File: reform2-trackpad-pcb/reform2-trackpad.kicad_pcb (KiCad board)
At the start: 2 copper layers, 45 x 21 mm, 26 parts, among them J1 Conn_USB, J2 Conn_01x06_Female, SW6 SW_RST, SW7 SW_HWB, U1 ATmega32U2-AU, U2 TLV75533PDBV, U3 USBLC6-2SC6, Y1 Crystal_GND24

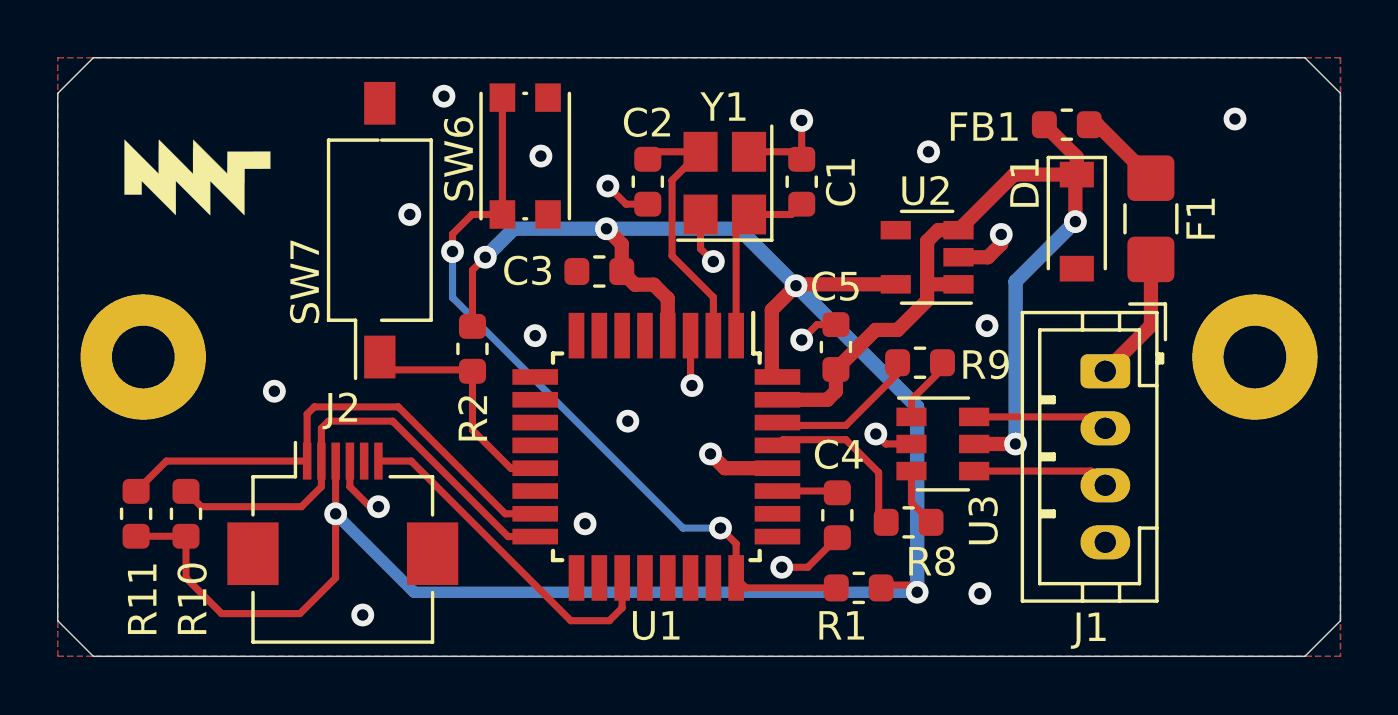
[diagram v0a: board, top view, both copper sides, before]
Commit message: reform2: update PCBs incl. badges to production revs, add keyboard lettering, misc docs
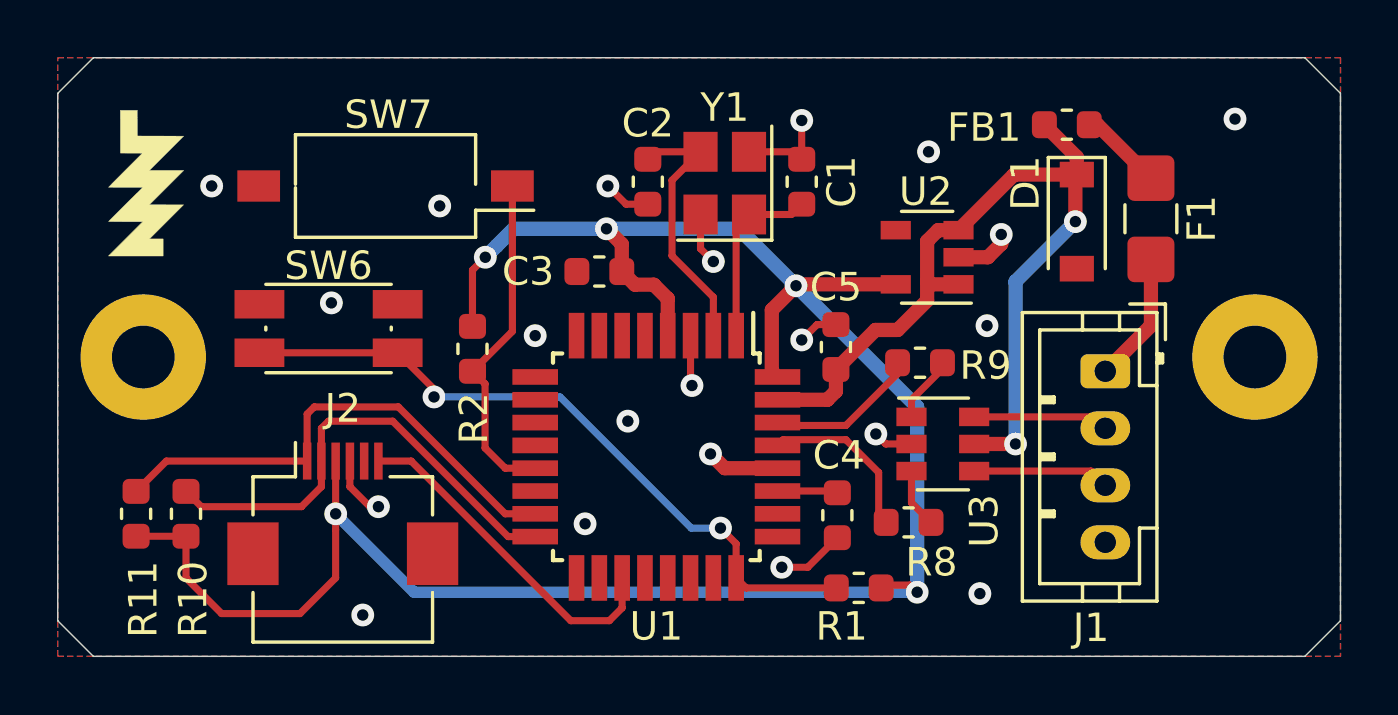
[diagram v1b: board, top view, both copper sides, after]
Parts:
- SW6: footprint Button_Switch_SMD:SW_Push_1P1T_NO_CK_KMR2 -> footprints2:Diptronics-PTLP2
- moved SW6 9.18 mm to (183.0, 104.5), turned to 0 degrees
- moved MK13 1.81 mm to (176.6, 99.4), turned to 90 degrees
- moved SW7 1.56 mm to (185.0, 99.5), turned to 180 degrees
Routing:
- net Net-(R2-Pad1): track 8.27 -> 12.1 mm
- net Net-(R1-Pad2): track 26.7 -> 24.5 mm
- net GND: vias 22 -> 21
